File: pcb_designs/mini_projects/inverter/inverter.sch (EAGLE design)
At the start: 8 parts, among them IC1 4047, Q1 IRFZ44, Q2 IRFZ44

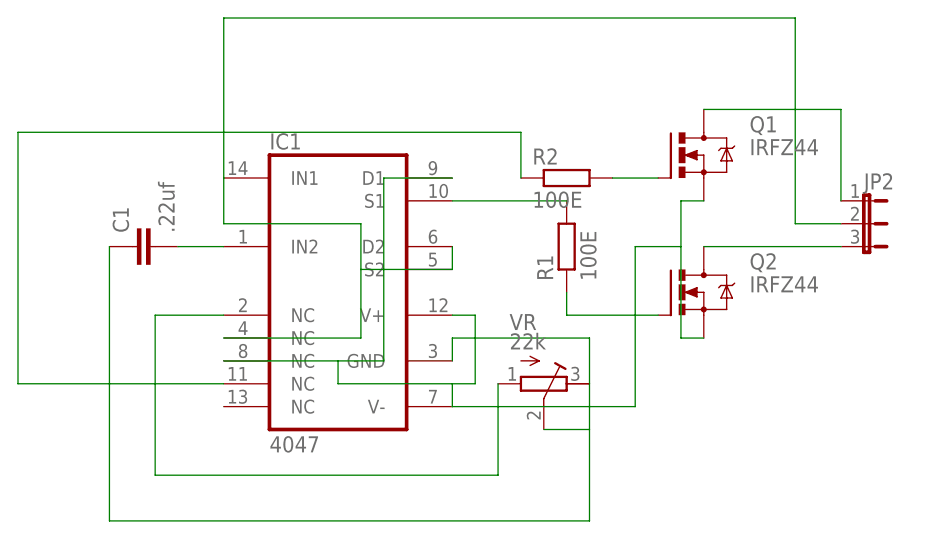
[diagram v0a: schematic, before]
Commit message: 
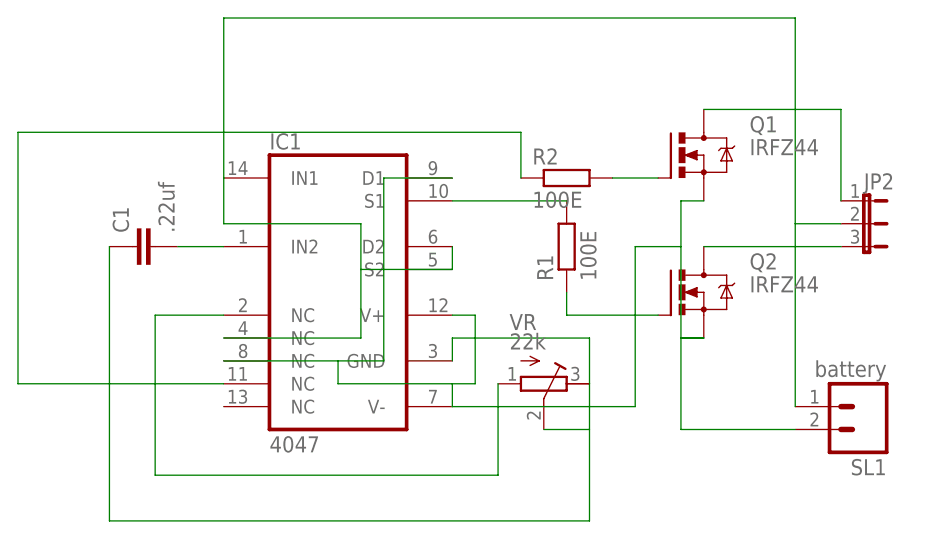
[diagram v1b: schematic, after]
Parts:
- added SL1: battery, con-amp-quick:M02
- C1: device capacitor-wima:C2.5/2 -> capacitor-wima:C5/3.5
- R1, R2: device rcl:R-EU_0204/7 -> rcl:R-EU_0207/15
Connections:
- net N$5: now also SL1.2
- net N$8: now also SL1.1
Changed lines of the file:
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@@
 <part name="Q1" library="transistor-power" deviceset="IRFZ48" device="Z" value="IRFZ44"/>
 <part name="Q2" library="transistor-power" deviceset="IRFZ48" device="Z" value="IRFZ44"/>
-<part name="R1" library="rcl" deviceset="R-EU_" device="0204/7" value="100E"/>
-<part name="R2" library="rcl" deviceset="R-EU_" device="0204/7" value="100E"/>
-<part name="C1" library="capacitor-wima" deviceset="C" device="2.5/2" value=".22uf"/>
+<part name="R1" library="rcl" deviceset="R-EU_" device="0207/15" value="100E"/>
+<part name="R2" library="rcl" deviceset="R-EU_" device="0207/15" value="100E"/>
+<part name="C1" library="capacitor-wima" deviceset="C" device="5/3.5" value=".22uf"/>
 <part name="VR" library="resistor" deviceset="R-TRIMM" device="64P" value="22k"/>
 <part name="JP2" library="jumper" deviceset="JP2E" device=""/>
+<part name="SL1" library="con-amp-quick" deviceset="M02" device="" value="battery"/>
 </parts>
 <sheets>
@@
 <instance part="VR" gate="G$1" x="63.5" y="53.34" rot="R270"/>
 <instance part="JP2" gate="1" x="99.06" y="71.12" rot="R270"/>
+<instance part="SL1" gate="G$1" x="99.06" y="50.8" rot="R180"/>
 </instances>
 <busses>
@@
 <pinref part="IC1" gate="G$1" pin="V+"/>
 <wire x1="55.88" y1="60.96" x2="53.34" y2="60.96" width="0.1524" layer="91"/>
+<wire x1="81.28" y1="58.42" x2="78.74" y2="58.42" width="0.1524" layer="91"/>
+<wire x1="78.74" y1="58.42" x2="78.74" y2="48.26" width="0.1524" layer="91"/>
+<pinref part="SL1" gate="G$1" pin="2"/>
+<wire x1="78.74" y1="48.26" x2="91.44" y2="48.26" width="0.1524" layer="91"/>
 </segment>
 </net>
@@
 <pinref part="JP2" gate="1" pin="2"/>
 <wire x1="91.44" y1="71.12" x2="96.52" y2="71.12" width="0.1524" layer="91"/>
+<pinref part="SL1" gate="G$1" pin="1"/>
+<wire x1="91.44" y1="71.12" x2="91.44" y2="50.8" width="0.1524" layer="91"/>
 </segment>
 </net>
